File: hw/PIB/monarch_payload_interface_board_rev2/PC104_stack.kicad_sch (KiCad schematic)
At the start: 30 parts, among them U1 Payload, U10 AD7124-8BCPZ-RL, U11 WSK06121L000FEA, U12 WSK06121L000FEA, U13 WSK06121L000FEA

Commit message: Schematic Clean Up + New Micro-Lock Plus Connectors
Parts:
- added C69: 0.1u, Capacitor_SMD:C_0603_1608Metric, symbol Device:C_Small
- U10: footprint AD7124:CP-32-12_ADI-L -> CP-32-12_ADI
- U11, U12, U13: footprint WSK:SMT_121L000FEA_VIS -> SMT_121L000FEA_VIS
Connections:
- net +3V3: now also C69.1
- net GND: now also U10.33 (EP), C69.2

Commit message: AD7124 Fixes
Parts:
- added R65: 10k, Resistor_SMD:R_0603_1608Metric, symbol Device:R_Small
- R60, R64: value ? -> 1000
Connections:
- net +3V3: now also R65.2
- net *SYNC: now reaches U10.27 (*SYNC)
- net *SYNC: now also R65.1
- no-connect marks 0 -> 11
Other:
- moved on the sheet: C48, C49, C55, C56, C57, C58, C59, C69, U10

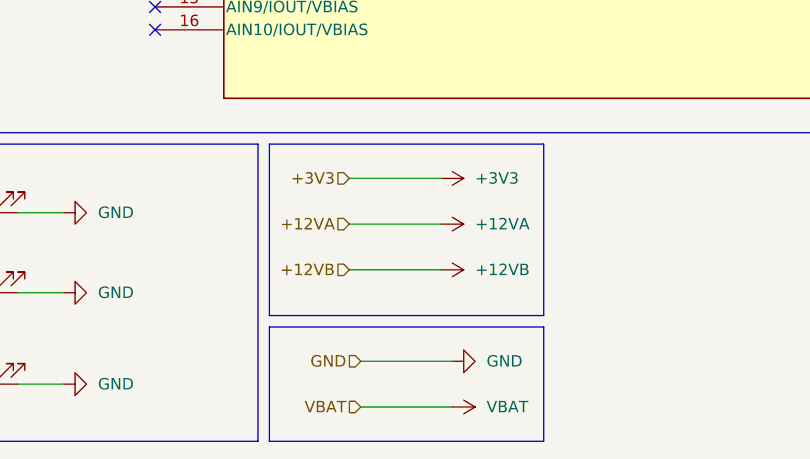
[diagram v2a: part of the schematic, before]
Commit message: Connector Footprints / Additions + Validated MAX31856
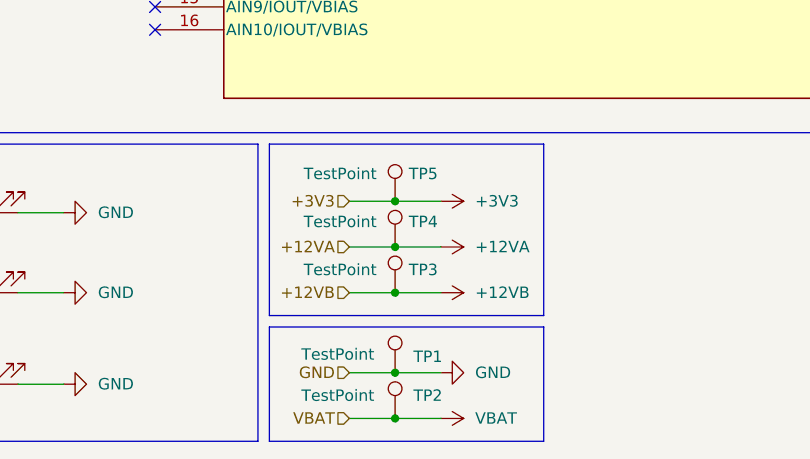
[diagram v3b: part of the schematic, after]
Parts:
- added TP1, TP2, TP3, TP4, TP5: TestPoint, symbol Connector:TestPoint
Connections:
- net +12VA: now also TP4.1
- net +12VB: now also TP3.1
- net +3V3: now also TP5.1
- net GND: now also TP1.1
- net VBAT: now also TP2.1

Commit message: AD7124 fixes
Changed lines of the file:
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@@
 		(in_pos_files yes)
 		(dnp no)
-		(fields_autoplaced yes)
 		(property "Reference" "#PWR0198"
 			(at 80.01 97.79 0)
@@
 		)
 		(property "Value" "GND"
-			(at 80.01 99.06 0)
+			(at 80.01 100.076 0)
 			(show_name no)
 			(do_not_autoplace no)

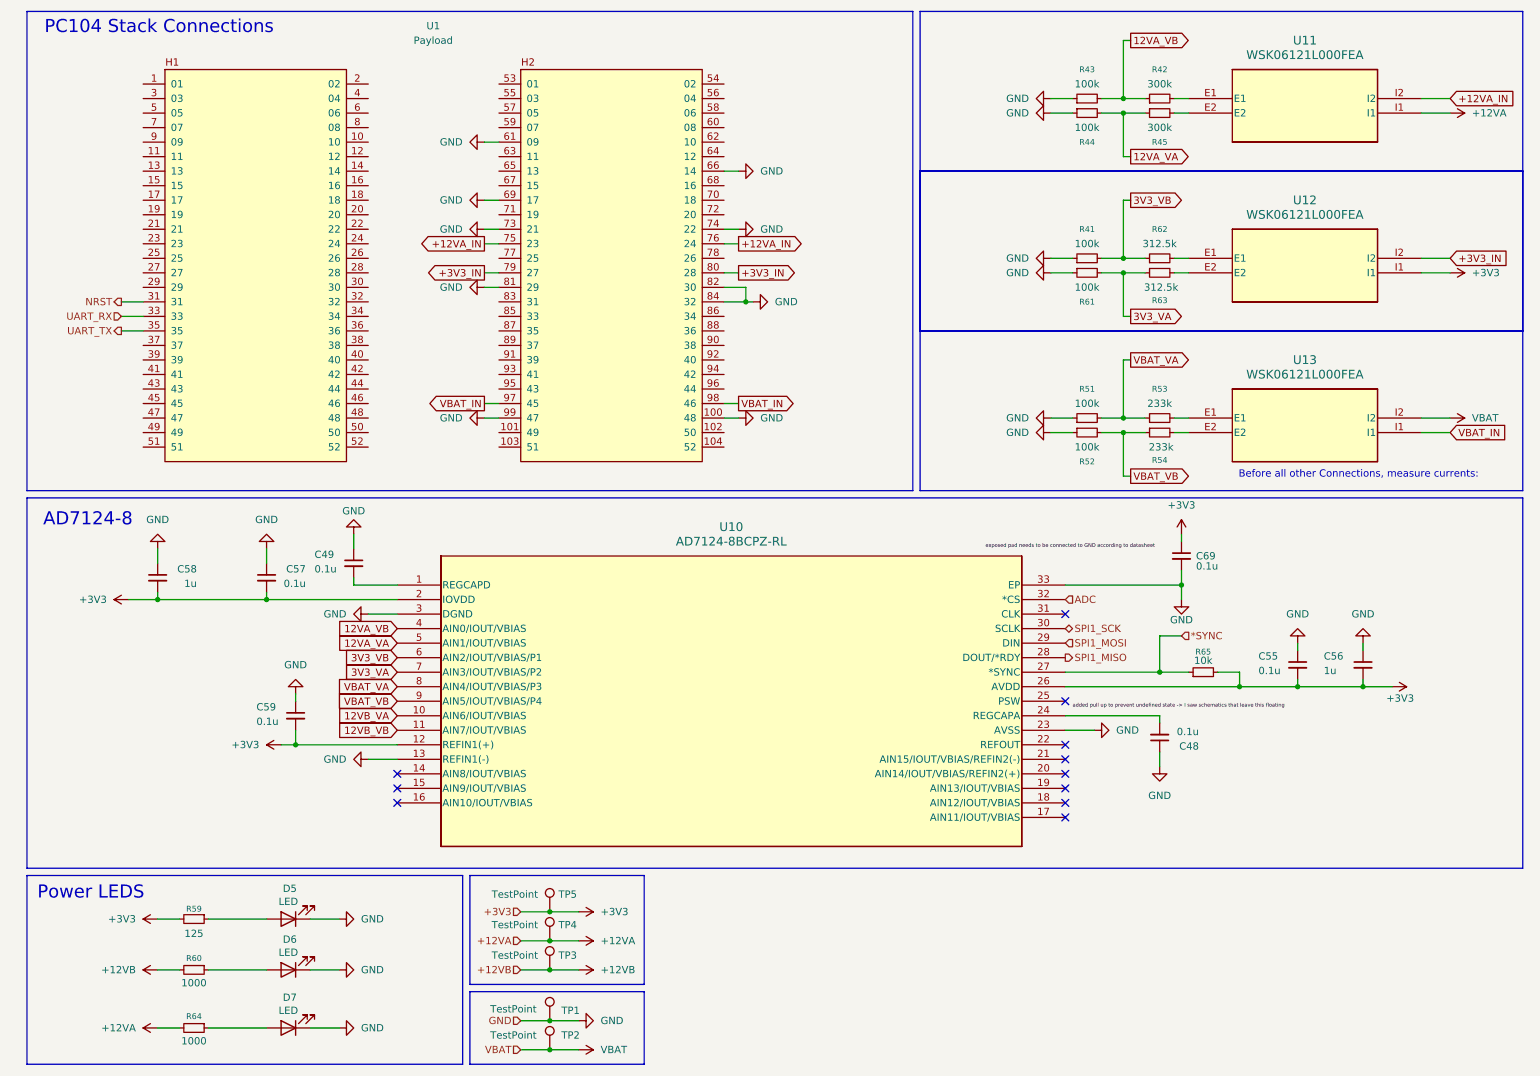
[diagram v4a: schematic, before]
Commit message: Schematic Updates Finished -> AD7124 Voltage Reading Fix + Connector Linkage Issue Fix
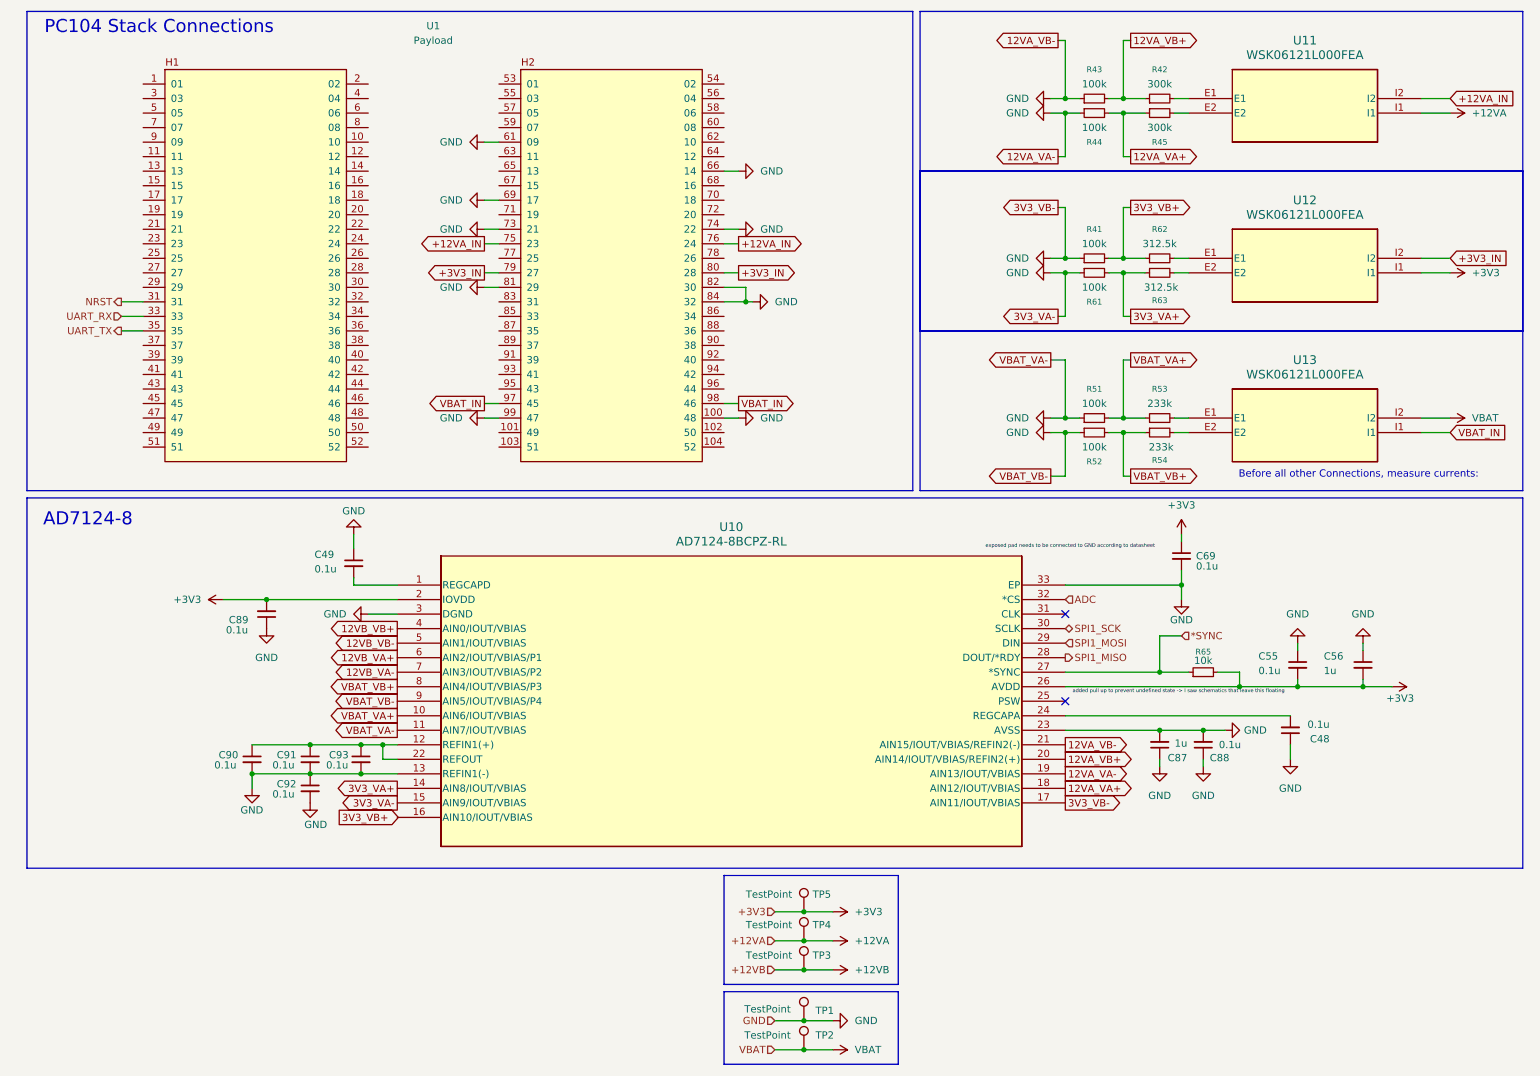
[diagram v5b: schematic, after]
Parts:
- removed C57, C59: 0.1u, Capacitor_SMD:C_0603_1608Metric, symbol Device:C_Small
- removed C58: 1u, Capacitor_SMD:C_0603_1608Metric, symbol Device:C_Small
- removed D5, D6, D7: LED, LED_SMD:LED_0603_1608Metric, symbol Device:LED
- removed R59: 125, Resistor_SMD:R_0603_1608Metric, symbol Device:R_Small
- removed R60, R64: 1000, Resistor_SMD:R_0603_1608Metric, symbol Device:R_Small
- added C87: 1u, Capacitor_SMD:C_0603_1608Metric, symbol Device:C_Small
- added C88, C89, C90, C91, C92, C93: 0.1u, Capacitor_SMD:C_0603_1608Metric, symbol Device:C_Small
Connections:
- net 12VB_VB is gone; now on net GND: U10.11 (AIN7/IOUT/VBIAS)
- net +3V3: now also C89.2; no longer U10.12 (REFIN1(+))
- net GND: now also U10.15 (AIN9/IOUT/VBIAS), U10.17 (AIN11/IOUT/VBIAS), U10.19 (AIN13/IOUT/VBIAS), U10.21 (AIN15/IOUT/VBIAS/REFIN2(-)), U10.9 (AIN5/IOUT/VBIAS/P4), C87.1, C87.2, C88.1, C88.2, C89.1, C90.2, C91.2, C92.1, C92.2, C93.2
- net 3V3_VA+: now reaches U10.14 (AIN8/IOUT/VBIAS)
- net 3V3_VA+: now also R61.2, R63.1
- net 12VA_VA+: now reaches U10.18 (AIN12/IOUT/VBIAS)
- net 12VA_VA+: now also R44.2, R45.1
- net 12VA_VB+: now reaches U10.20 (AIN14/IOUT/VBIAS/REFIN2(+))
- net 12VA_VB+: now also R42.1, R43.2
- net at U10.22 (REFOUT): now also U10.12 (REFIN1(+)), C90.1, C91.1, C93.1
- removed net 12VA_VA: R44.2, R45.1, U10.5 (AIN1/IOUT/VBIAS)
- removed net 12VA_VB: R42.1, R43.2, U10.4 (AIN0/IOUT/VBIAS)
- net 12VB_VA renamed VBAT_VA+
- net VBAT_VA+: now also R51.2, R53.1
- removed net 3V3_VA: R61.2, R63.1, U10.7 (AIN3/IOUT/VBIAS/P2)
- net 3V3_VB renamed 3V3_VB+
- net 3V3_VB+: no longer U10.6 (AIN2/IOUT/VBIAS/P1)
- removed net VBAT_VA: R51.2, R53.1, U10.8 (AIN4/IOUT/VBIAS/P3)
- net VBAT_VB renamed VBAT_VB+
- net VBAT_VB+: now also U10.8 (AIN4/IOUT/VBIAS/P3); no longer U10.9 (AIN5/IOUT/VBIAS/P4)
- new net 12VB_VA+: U10.6 (AIN2/IOUT/VBIAS/P1)
- new net 12VB_VA-: U10.7 (AIN3/IOUT/VBIAS/P2)
- new net 12VB_VB+: U10.4 (AIN0/IOUT/VBIAS)
- new net 12VB_VB-: U10.5 (AIN1/IOUT/VBIAS)
- no-connect marks 11 -> 2
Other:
- note removed: "Power LEDS"
- moved on the sheet: C48, R41, R43, R44, R51, R52, R61, TP1, TP2, TP3, TP4, TP5

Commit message: Footprint Selected
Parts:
- TP1, TP2, TP3, TP4, TP5: footprint (none) -> TestPoint:TestPoint_Pad_D1.0mm
- U10: footprint CP-32-12_ADI -> AD7124:CP-32-12_ADI
- U11, U12, U13: footprint SMT_121L000FEA_VIS -> WSK:SMT_121L000FEA_VIS
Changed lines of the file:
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@@
 			)
 		)
-		(property "Footprint" ""
+		(property "Footprint" "TestPoint:TestPoint_Pad_D1.0mm"
 			(at 163.83 175.26 0)
 			(hide yes)
@@
 			)
 		)
-		(property "Footprint" "SMT_121L000FEA_VIS"
+		(property "Footprint" "WSK:SMT_121L000FEA_VIS"
 			(at 226.06 27.94 0)
 			(hide yes)
@@
 			)
 		)
-		(property "Footprint" ""
+		(property "Footprint" "TestPoint:TestPoint_Pad_D1.0mm"
 			(at 163.83 170.18 0)
 			(hide yes)
@@
 			)
 		)
-		(property "Footprint" "SMT_121L000FEA_VIS"
+		(property "Footprint" "WSK:SMT_121L000FEA_VIS"
 			(at 226.06 55.88 0)
 			(hide yes)
@@
 			)
 		)
-		(property "Footprint" "CP-32-12_ADI"
+		(property "Footprint" "AD7124:CP-32-12_ADI"
 			(at 87.63 113.03 0)
 			(hide yes)
@@
 			)
 		)
-		(property "Footprint" ""
+		(property "Footprint" "TestPoint:TestPoint_Pad_D1.0mm"
 			(at 163.83 180.34 0)
 			(hide yes)
@@
 			)
 		)
-		(property "Footprint" "SMT_121L000FEA_VIS"
+		(property "Footprint" "WSK:SMT_121L000FEA_VIS"
 			(at 226.06 83.82 0)
 			(hide yes)
@@
 			)
 		)
-		(property "Footprint" ""
+		(property "Footprint" "TestPoint:TestPoint_Pad_D1.0mm"
 			(at 163.83 189.23 0)
 			(hide yes)
@@
 			)
 		)
-		(property "Footprint" ""
+		(property "Footprint" "TestPoint:TestPoint_Pad_D1.0mm"
 			(at 163.83 194.31 0)
 			(hide yes)
